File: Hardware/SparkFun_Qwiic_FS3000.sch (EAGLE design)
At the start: 26 parts, among them J2 QWIIC_RA, U1 FS3000

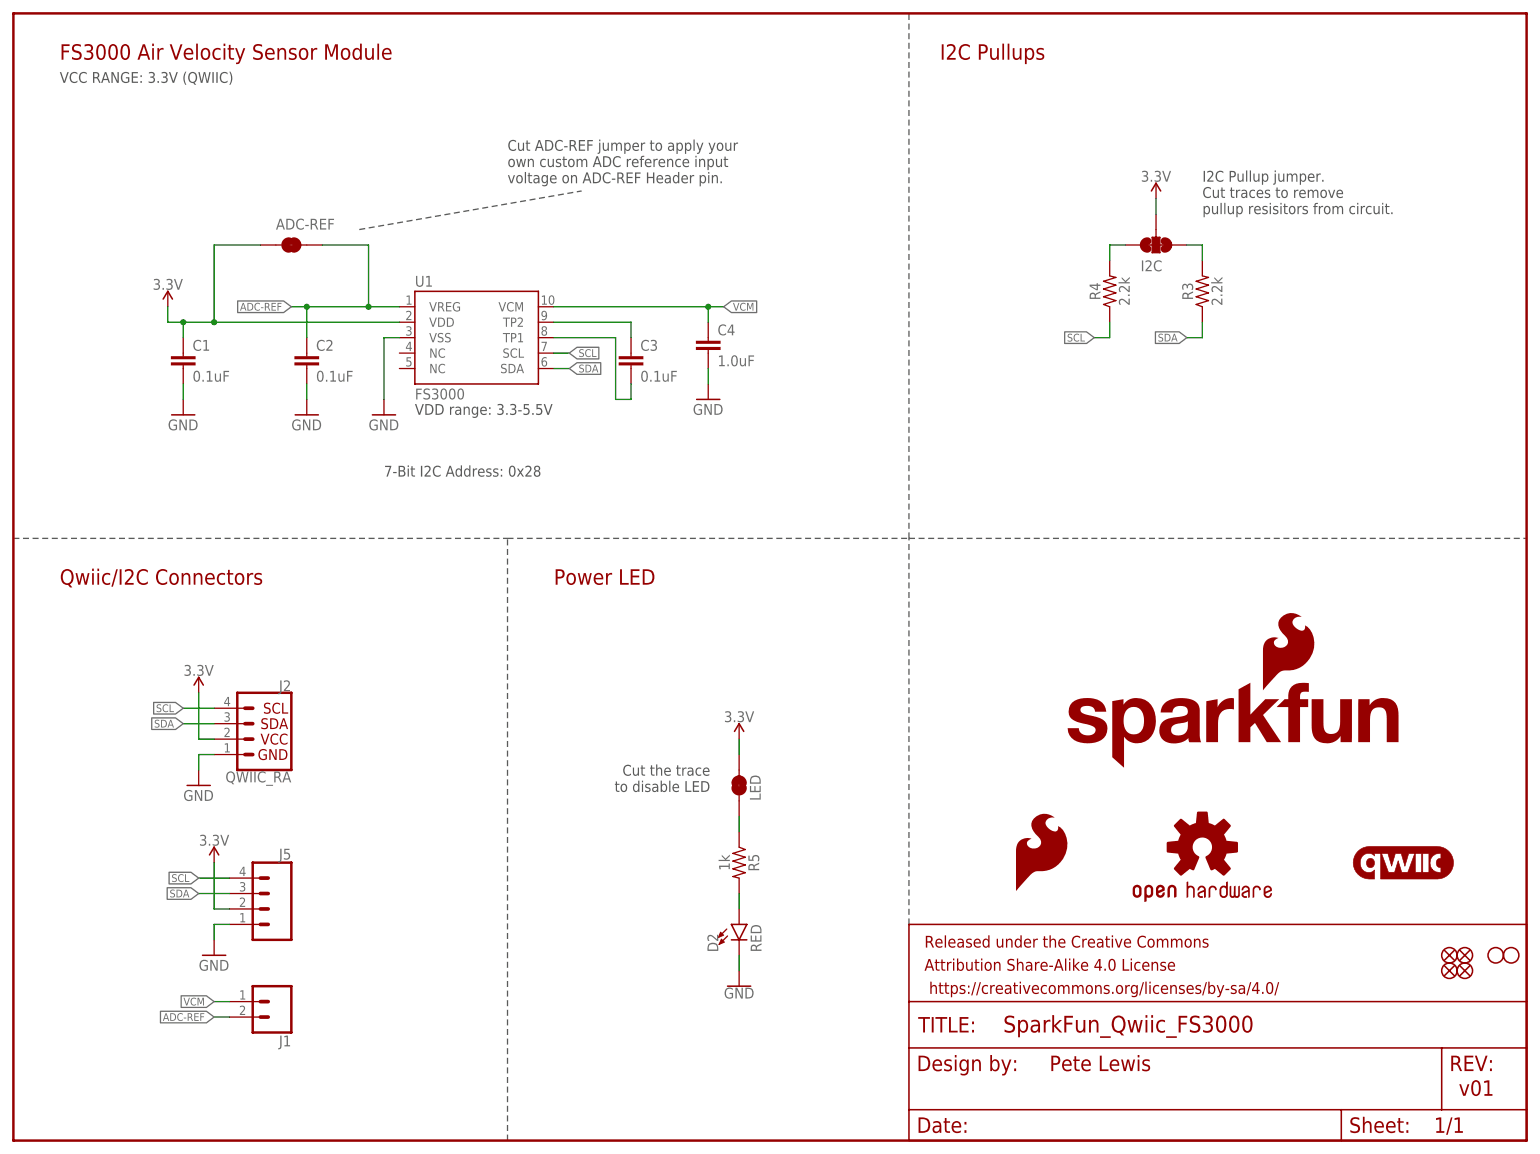
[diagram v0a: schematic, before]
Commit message: Decided to use 1X1 version, bumped version to "v10"
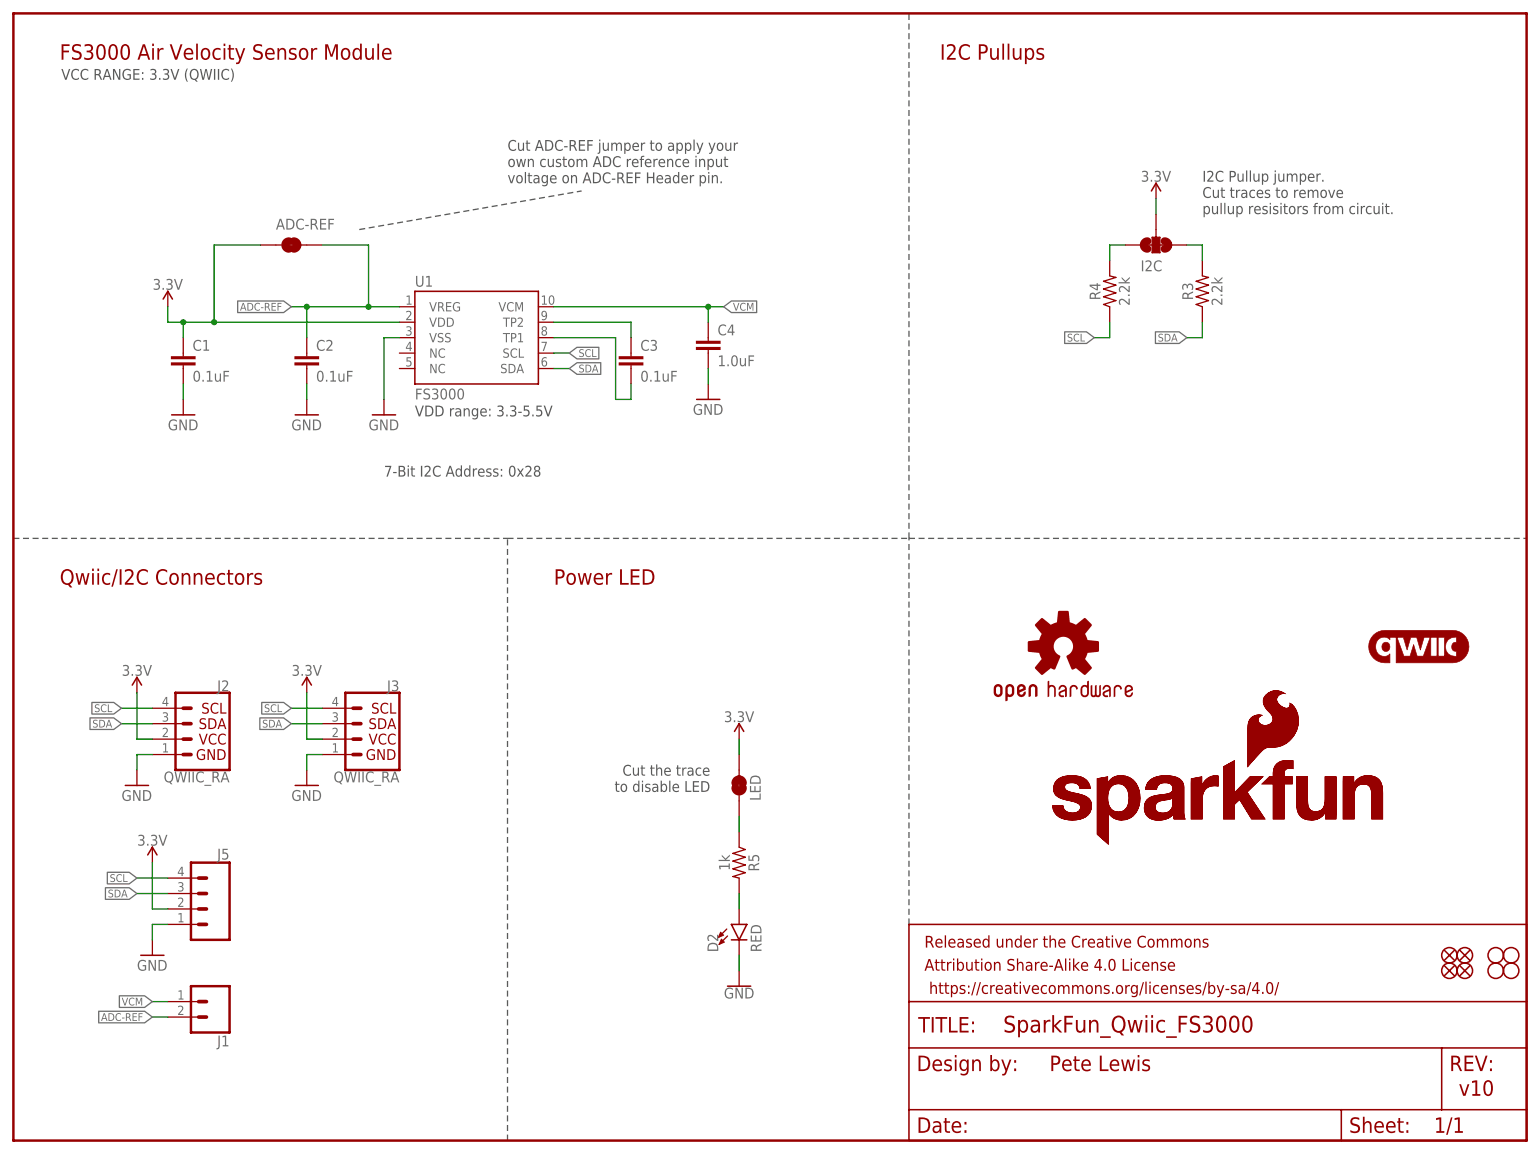
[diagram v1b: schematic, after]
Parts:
- added J3: QWIIC_RA, SparkFun-Connectors:QWIIC_CONNECTORJS-1MM
- added JP4, JP7: STAND-OFF, SparkFun-Hardware:STAND-OFF
- LOGO3: value SFE_LOGO_FLAME.1_INCH -> SFE_LOGO_NAME_FLAME.1_INCH; device SparkFun-Aesthetics:SFE_LOGO_FLAME.1_INCH -> SparkFun-Aesthetics:SFE_LOGO_NAME_FLAME.1_INCH
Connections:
- net 3.3V: now also J3.2
- net GND: now also J3.1
- net SCL: now also J3.4
- net SDA: now also J3.3
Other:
- note added: "v10"
- note removed: "v01"
- moved on the sheet: J1, J2, J5
